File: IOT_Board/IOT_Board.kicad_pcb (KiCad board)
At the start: 2 copper layers, 57 parts, among them J1 Screw_Terminal_01x03, J10 Conn_02x04_Counter_Clockwise, J2 Screw_Terminal_01x03, J3 Conn_02x10_Counter_Clockwise, J4 Conn_02x10_Counter_Clockwise, J5 Screw_Terminal_01x03, J6 Screw_Terminal_01x03, J7 Screw_Terminal_01x05, J8 Screw_Terminal_01x03, J9 analog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

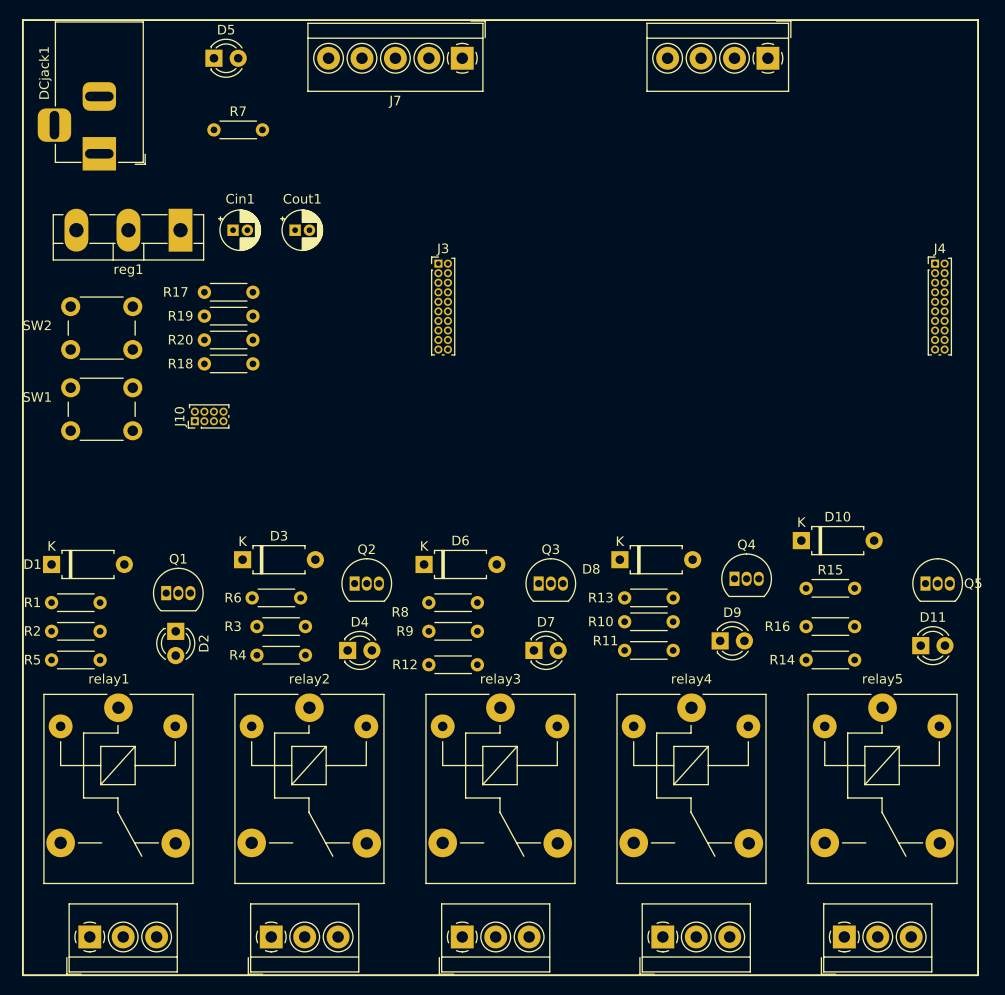
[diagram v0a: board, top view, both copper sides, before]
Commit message: layout for TIVA board
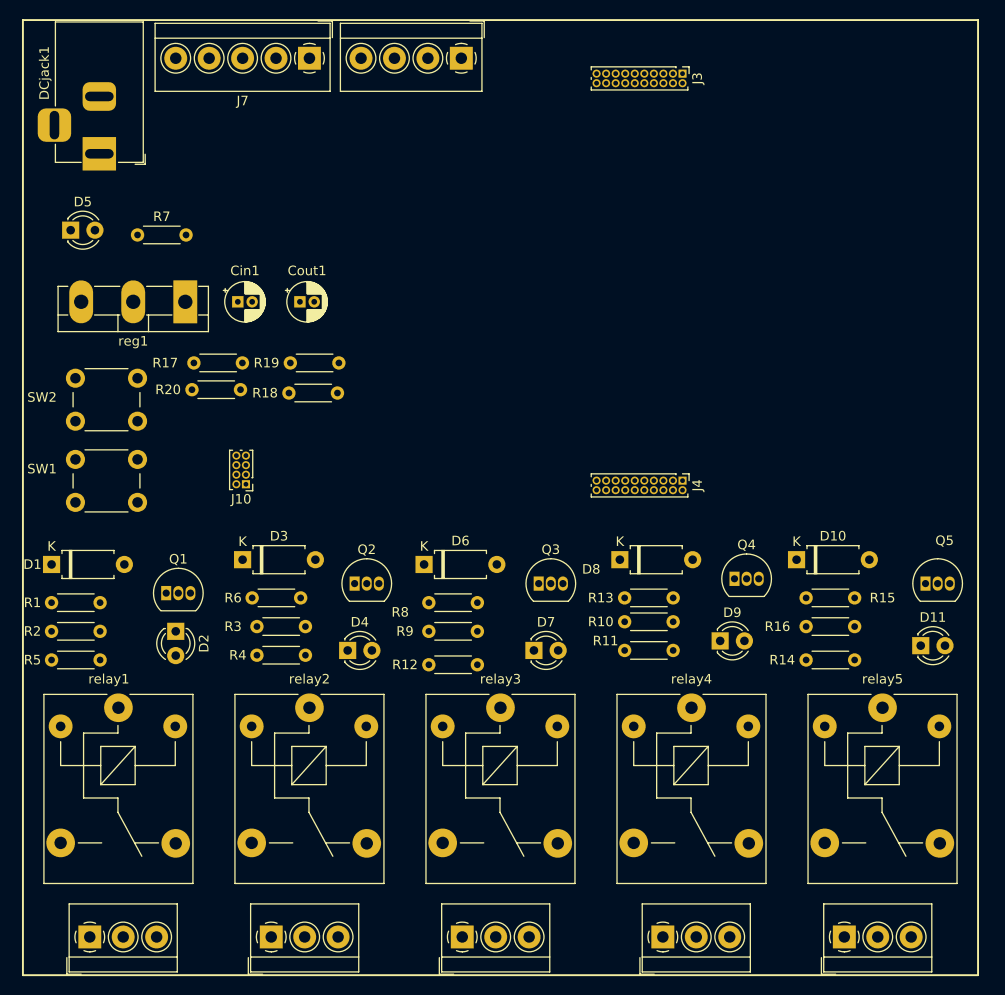
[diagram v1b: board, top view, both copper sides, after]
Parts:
- moved J4 34.9 mm to (139.1, 98.2), turned to 270 degrees
- moved J3 32.4 mm to (139.1, 55.6), turned to 270 degrees
- moved J9 32.1 mm to (115.9, 54.0)
- moved D5 23.4 mm to (75.0, 72.0)
- moved J7 16.0 mm to (100.0, 54.0)
- moved R7 13.6 mm to (82.0, 72.5)
- moved R19 10.2 mm to (98.0, 85.9)
- moved R18 9.36 mm to (97.8, 89.0)
- moved J10 8.50 mm to (93.3, 98.6), turned to 180 degrees
- moved Cin1 7.52 mm to (92.5, 79.5)
- moved Cout1 7.52 mm to (99.0, 79.5)
- moved SW1 7.52 mm to (75.5, 96.0)
- moved SW2 7.52 mm to (75.5, 87.5)
- moved reg1 7.52 mm to (87.0, 79.5)
- moved R17 7.48 mm to (87.9, 85.9)
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
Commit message: added tracks, produced gerber files
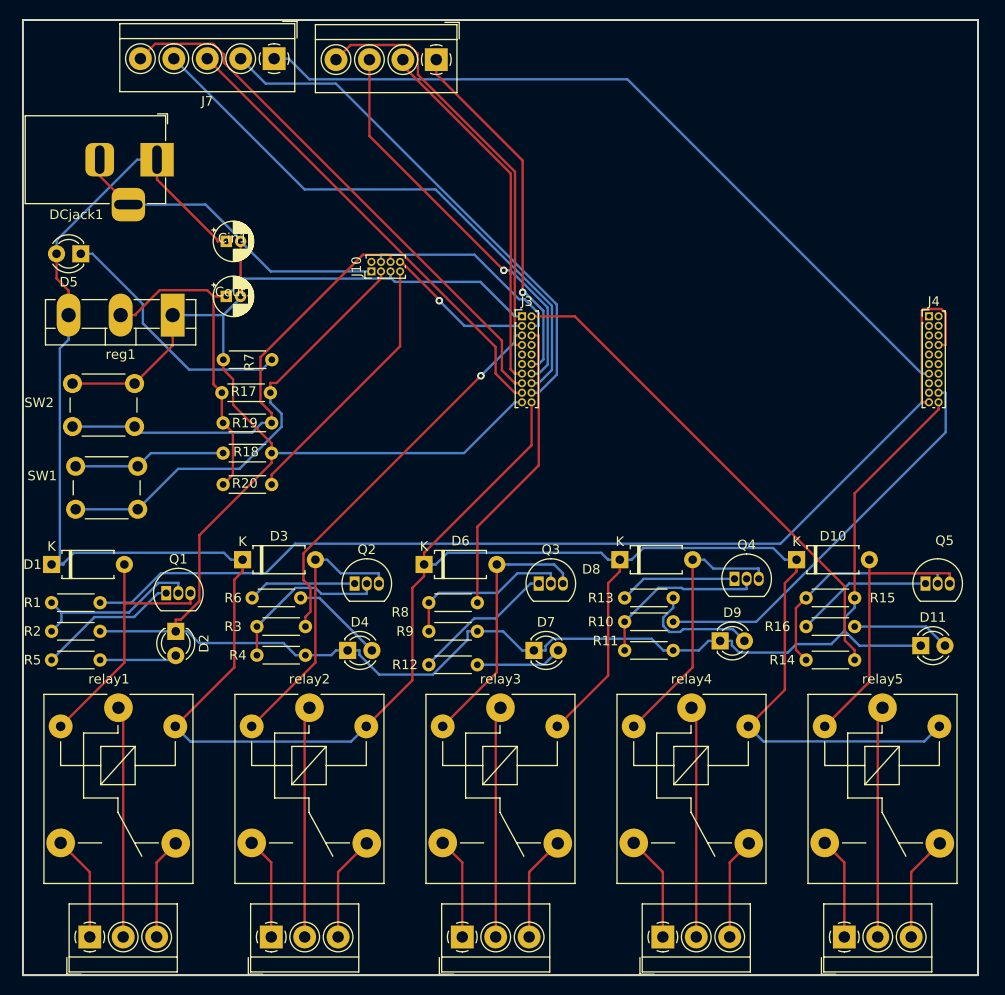
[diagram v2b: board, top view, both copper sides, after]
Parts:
- moved J4 31.0 mm to (164.9, 81.0), turned to 0 degrees
- moved J3 30.5 mm to (122.3, 81.0), turned to 0 degrees
- moved J10 25.9 mm to (106.5, 76.3), turned to 90 degrees
- moved R7 19.2 mm to (96.1, 85.6), turned to 180 degrees
- moved R20 10.5 mm to (91.0, 98.6)
- moved R19 9.43 mm to (91.0, 92.2)
- moved R18 9.33 mm to (91.0, 95.3)
- moved Cout1 7.73 mm to (91.3, 78.9)
- moved Cin1 6.44 mm to (91.3, 73.2)
- moved DCjack1 6.07 mm to (84.0, 64.6), turned to 0 degrees
- moved R17 4.28 mm to (90.8, 89.0)
- moved J7 3.70 mm to (96.3, 54.0)
- moved D5 2.69 mm to (76.1, 74.5), turned to 180 degrees
- moved J9 2.62 mm to (113.3, 54.1)
- moved reg1 1.92 mm to (85.7, 80.9)
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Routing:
- net /vcc5v: track 0.00 -> 266.7 mm
- net GND: track 0.00 -> 255.4 mm
- net /s0: track 0.00 -> 112.6 mm
- net /ch0: track 0.00 -> 82.2 mm
- net /vcc3v3: track 0.00 -> 67.5 mm
- net /ch3: track 0.00 -> 59.7 mm
- net /ch4: track 0.00 -> 57.6 mm
- net /ch1: track 0.00 -> 54.5 mm
- net /s2: track 0.00 -> 52.6 mm
- net /ch2: track 0.00 -> 49.1 mm
- net /rs: track 0.00 -> 47.7 mm
- net /io0: track 0.00 -> 47.1 mm
- net /an10: track 0.00 -> 45.0 mm
- net /an2: track 0.00 -> 42.2 mm, vias 0 -> 1
- net /s1: track 0.00 -> 41.6 mm
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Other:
- board outline added: 100 x 100 mm
- rule trace_min: 0.2 -> 0.1524
- rule via_min_drill: 0.3 -> 0.254
- rule via_min_size: 0.4 -> 0.254
